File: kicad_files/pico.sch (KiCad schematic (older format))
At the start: 66 parts, among them K0 KEYSW, K1 KEYSW, K10 KEYSW, K11 KEYSW, K12 KEYSW, K13 KEYSW, K14 KEYSW, K15 KEYSW, K2 KEYSW, K20 KEYSW, K21 KEYSW, K22 KEYSW, K23 KEYSW, K24 KEYSW, K25 KEYSW, K3 KEYSW, K30 KEYSW, K31 KEYSW, K32 KEYSW, K33 KEYSW, K34 KEYSW, K35 KEYSW, K4 KEYSW, K40 KEYSW, K41 KEYSW, K42 KEYSW, K43 KEYSW, K44 KEYSW, K45 KEYSW, K5 KEYSW, U1 ProMicro

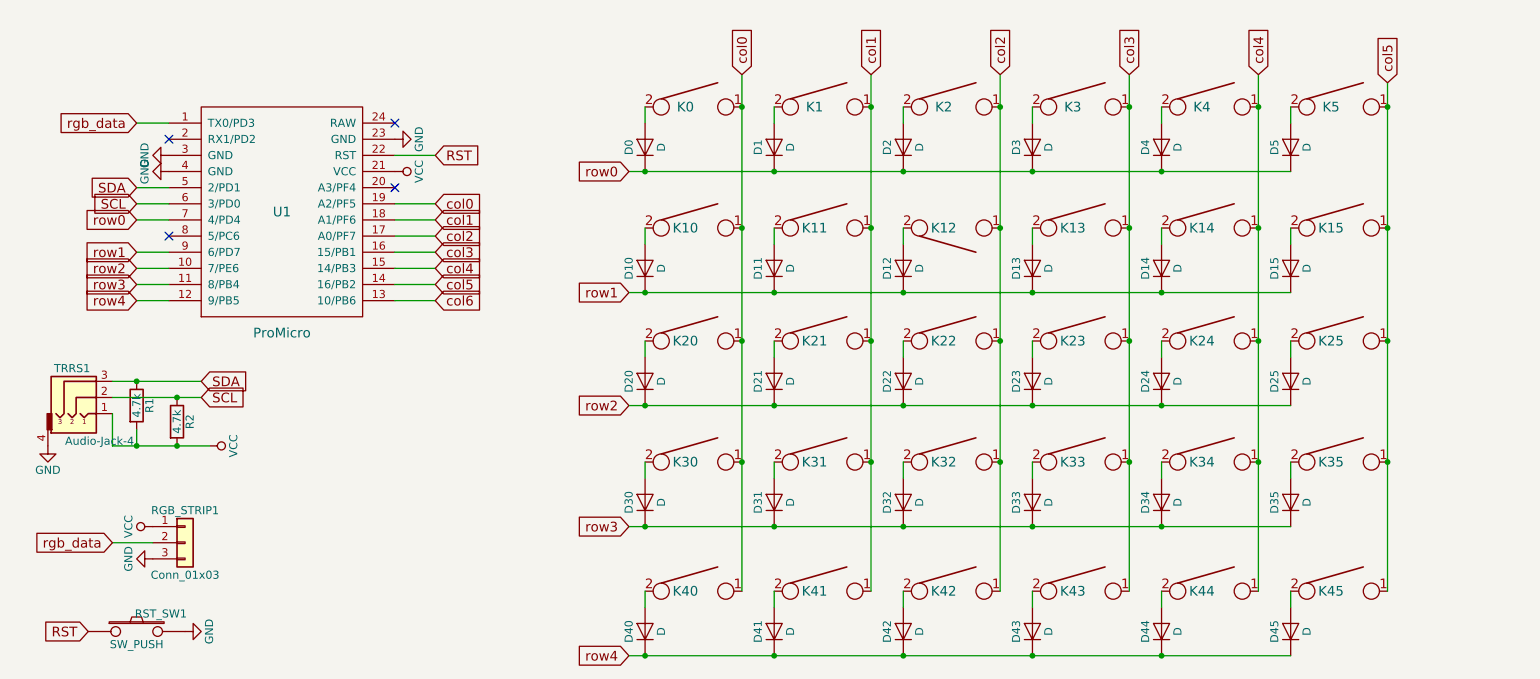
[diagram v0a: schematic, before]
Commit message: Modified outline of pico keyboard.
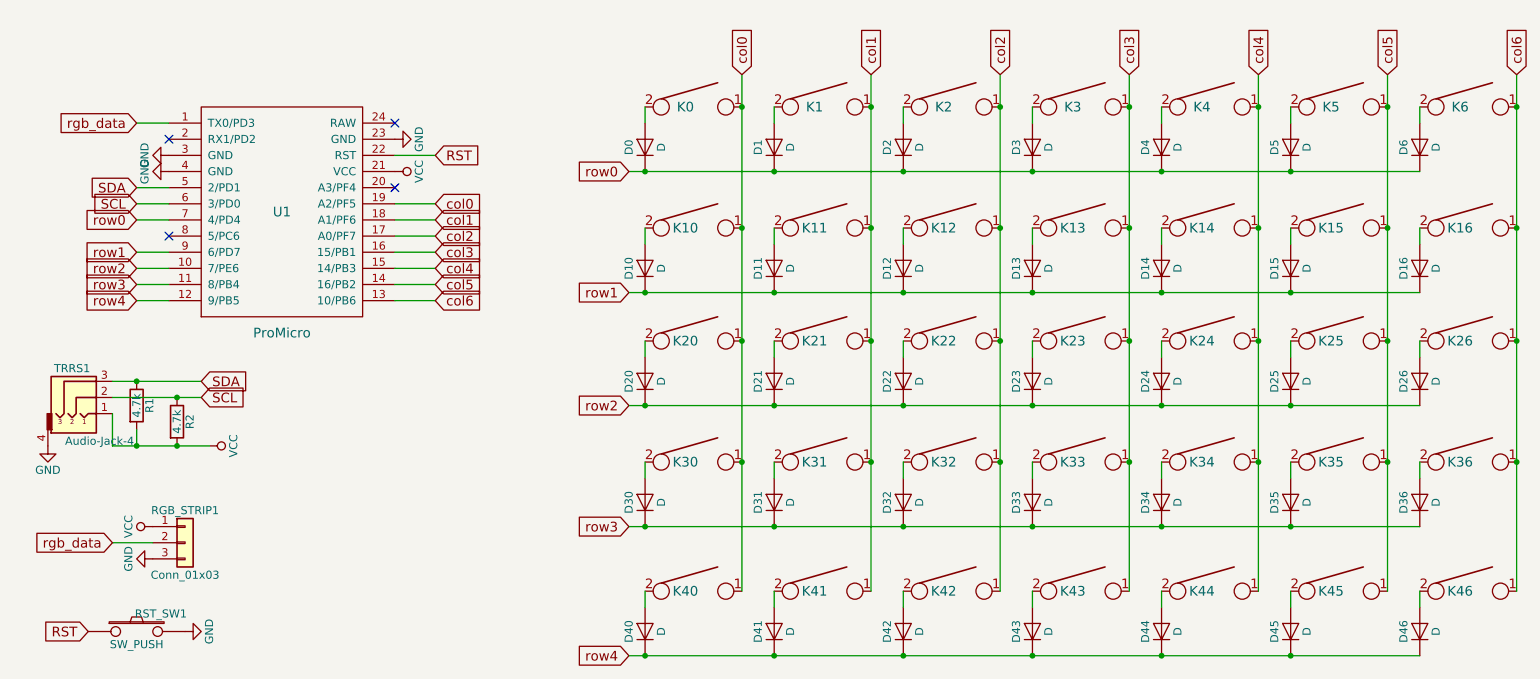
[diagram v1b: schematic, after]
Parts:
- added D16, D26, D36, D46, D6: D, pico_footprints:Diode-dual, symbol pico:D
- added K16, K26, K36, K46, K6: KEYSW, pico_footprints:Kailh_mid_height, symbol pico:KEYSW
- D0, D1, D10, D11, D12, D13, D14, D15, D2, D20, D21, D22, D23, D24, D25, D3, D30, D31, D32, D33, D34, D35, D4, D40, D41, D42, D43, D44, D45, D5: footprint Keebio-Parts:Diode-dual -> pico_footprints:Diode-dual
- R1, R2: footprint Keebio-Parts:Resistor-Compact -> pico_footprints:Resistor-Compact
- RGB_STRIP1: footprint Pin_Headers:Pin_Header_Straight_1x03_Pitch2.54mm -> pico_footprints:Pin_Header_Straight_1x03_Pitch2.54mm
- RST_SW1: footprint Buttons_Switches_ThroughHole:SW_PUSH_6mm_h4.3mm -> pico_footprints:SW_PUSH_6mm_h4.3mm
- TRRS1: footprint Keebio-Parts:TRRS-PJ-320A-dual -> pico_footprints:TRRS-PJ-320A
- U1: footprint Keebio-Parts:ArduinoProMicro -> pico_footprints:ArduinoProMicro
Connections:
- net col6: now also K16.1, K26.1, K36.1, K46.1, K6.1
- net row0: now also D6.1 (K)
- net row1: now also D16.1 (K)
- net row2: now also D26.1 (K)
- net row3: now also D36.1 (K)
- net row4: now also D46.1 (K)
- new net: D6.2 (A), K6.2
- new net: D16.2 (A), K16.2
- new net: D26.2 (A), K26.2
- new net: D36.2 (A), K36.2
- new net: D46.2 (A), K46.2
